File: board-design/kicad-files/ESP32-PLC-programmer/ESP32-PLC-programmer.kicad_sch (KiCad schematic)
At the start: 28 parts, among them J1 302-S101, J2 0473460001, J3 302-S101, U1 TPS62060DSGR, U2 FT231XS

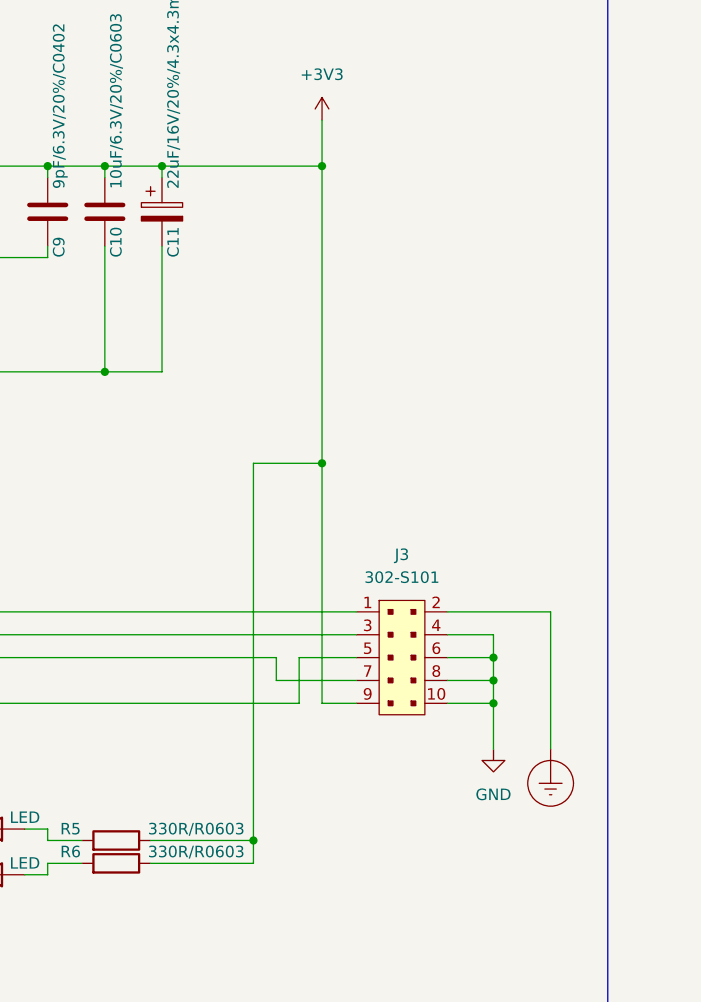
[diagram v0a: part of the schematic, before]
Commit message: [UPDATE]
Finished ESP32 and ESP32-programmer board designs (few corrections to be made when manufacturer is chosen - design rules).

Signed-off-by: Nicolae-Andrei Vasile <vasilenicolaeandrei@gmail.com>
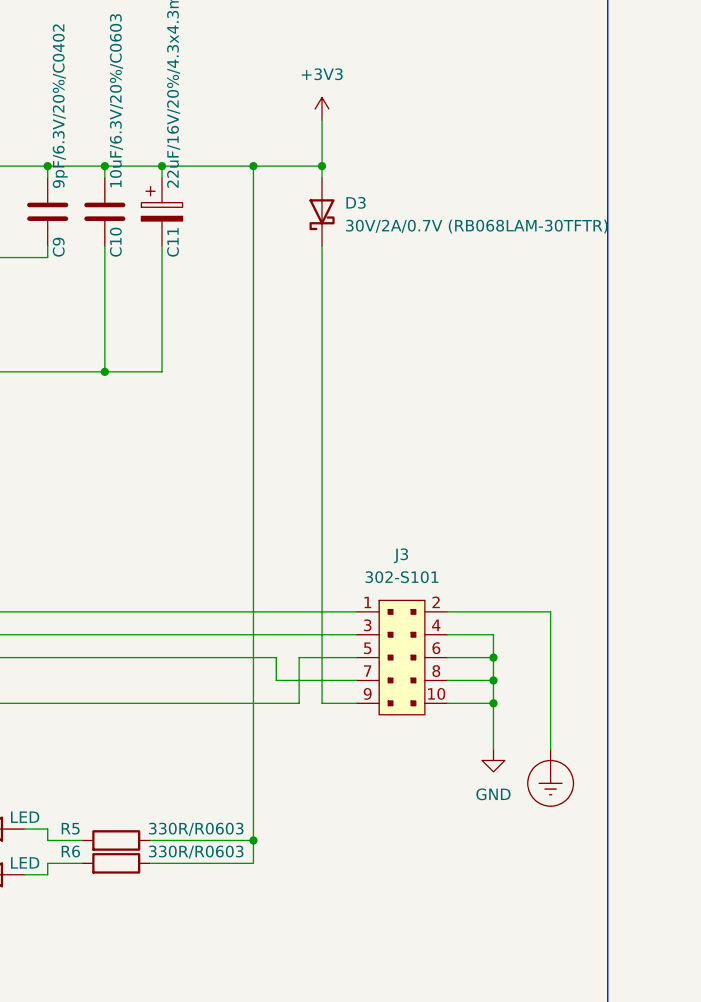
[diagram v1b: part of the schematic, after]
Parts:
- added D3: 30V/2A/0.7V (RB068LAM-30TFTR), Diode_SMD:D_SOD-128, symbol Device:D_Schottky
- J1, J3: footprint digikey-footprints:PinHeader_2x5_P2.54mm_Drill1.2mm -> Connector_IDC:IDC-Header_2x05_P2.54mm_Vertical
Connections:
- net +3V3: now also D3.2 (A); no longer J3.9
- new net: D3.1 (K), J3.9
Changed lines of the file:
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@@
   (junction (at 119.38 92.71) (diameter 0) (color 0 0 0 0)
   )
+  (junction (at 217.17 38.1) (diameter 0) (color 0 0 0 0)
+  )
+  (junction (at 113.03 132.08) (diameter 0) (color 0 0 0 0)
+  )
+  (junction (at 160.02 60.96) (diameter 0) (color 0 0 0 0)
+  )
+  (junction (at 195.58 38.1) (diameter 0) (color 0 0 0 0)
+  )
+  (junction (at 106.68 95.25) (diameter 0) (color 0 0 0 0)
+  )
+  (junction (at 80.01 132.08) (diameter 0) (color 0 0 0 0)
+  )
+  (junction (at 153.67 60.96) (diameter 0) (color 0 0 0 0)
+  )
+  (junction (at 254 92.71) (diameter 0) (color 0 0 0 0)
+  )
+  (junction (at 195.58 60.96) (diameter 0) (color 0 0 0 0)
+  )
+  (junction (at 227.33 113.03) (diameter 0) (color 0 0 0 0)
+  )
+  (junction (at 95.25 132.08) (diameter 0) (color 0 0 0 0)
+  )
+  (junction (at 119.38 132.08) (diameter 0) (color 0 0 0 0)
+  )
+  (junction (at 48.26 171.45) (diameter 0) (color 0 0 0 0)
+  )
+  (junction (at 125.73 77.47) (diameter 0) (color 0 0 0 0)
+  )
+  (junction (at 160.02 40.64) (diameter 0) (color 0 0 0 0)
+  )
+  (junction (at 210.82 60.96) (diameter 0) (color 0 0 0 0)
+  )
+  (junction (at 27.94 163.83) (diameter 0) (color 0 0 0 0)
+  )
+  (junction (at 27.94 173.99) (diameter 0) (color 0 0 0 0)
+  )
+  (junction (at 113.03 97.79) (diameter 0) (color 0 0 0 0)
+  )
+  (junction (at 160.02 38.1) (diameter 0) (color 0 0 0 0)
+  )
+  (junction (at 204.47 38.1) (diameter 0) (color 0 0 0 0)
+  )
+  (junction (at 227.33 38.1) (diameter 0) (color 0 0 0 0)
+  )
+  (junction (at 153.67 38.1) (diameter 0) (color 0 0 0 0)
+  )
   (junction (at 234.95 38.1) (diameter 0) (color 0 0 0 0)
-  )
-  (junction (at 217.17 38.1) (diameter 0) (color 0 0 0 0)
-  )
-  (junction (at 113.03 132.08) (diameter 0) (color 0 0 0 0)
-  )
-  (junction (at 160.02 60.96) (diameter 0) (color 0 0 0 0)
-  )
-  (junction (at 195.58 38.1) (diameter 0) (color 0 0 0 0)
-  )
-  (junction (at 106.68 95.25) (diameter 0) (color 0 0 0 0)
-  )
-  (junction (at 80.01 132.08) (diameter 0) (color 0 0 0 0)
-  )
-  (junction (at 153.67 60.96) (diameter 0) (color 0 0 0 0)
-  )
-  (junction (at 254 92.71) (diameter 0) (color 0 0 0 0)
-  )
-  (junction (at 195.58 60.96) (diameter 0) (color 0 0 0 0)
-  )
-  (junction (at 227.33 113.03) (diameter 0) (color 0 0 0 0)
-  )
-  (junction (at 95.25 132.08) (diameter 0) (color 0 0 0 0)
-  )
-  (junction (at 119.38 132.08) (diameter 0) (color 0 0 0 0)
-  )
-  (junction (at 48.26 171.45) (diameter 0) (color 0 0 0 0)
-  )
-  (junction (at 125.73 77.47) (diameter 0) (color 0 0 0 0)
-  )
-  (junction (at 160.02 40.64) (diameter 0) (color 0 0 0 0)
-  )
-  (junction (at 210.82 60.96) (diameter 0) (color 0 0 0 0)
-  )
-  (junction (at 27.94 163.83) (diameter 0) (color 0 0 0 0)
-  )
-  (junction (at 27.94 173.99) (diameter 0) (color 0 0 0 0)
-  )
-  (junction (at 113.03 97.79) (diameter 0) (color 0 0 0 0)
-  )
-  (junction (at 160.02 38.1) (diameter 0) (color 0 0 0 0)
-  )
-  (junction (at 204.47 38.1) (diameter 0) (color 0 0 0 0)
-  )
-  (junction (at 153.67 38.1) (diameter 0) (color 0 0 0 0)
-  )
-  (junction (at 234.95 71.12) (diameter 0) (color 0 0 0 0)
   )
   (junction (at 48.26 173.99) (diameter 0) (color 0 0 0 0)
@@
     (stroke (width 0) (type default))
   )
-  (wire (pts (xy 217.17 38.1) (xy 234.95 38.1))
+  (wire (pts (xy 217.17 38.1) (xy 227.33 38.1))
     (stroke (width 0) (type default))
   )
@@
     (stroke (width 0) (type default))
   )
+  (wire (pts (xy 227.33 38.1) (xy 234.95 38.1))
+    (stroke (width 0) (type default))
+  )
   (wire (pts (xy 170.18 80.01) (xy 170.18 77.47))
     (stroke (width 0) (type default))
@@
     (stroke (width 0) (type default))
   )
-  (wire (pts (xy 227.33 71.12) (xy 227.33 113.03))
+  (wire (pts (xy 227.33 38.1) (xy 227.33 113.03))
+    (stroke (width 0) (type default))
+  )
+  (wire (pts (xy 234.95 38.1) (xy 234.95 39.37))
     (stroke (width 0) (type default))
   )
@@
     (stroke (width 0) (type default))
   )
-  (wire (pts (xy 234.95 38.1) (xy 234.95 71.12))
-    (stroke (width 0) (type default))
-  )
   (wire (pts (xy 105.41 176.53) (xy 105.41 179.07))
     (stroke (width 0) (type default))
@@
     (stroke (width 0) (type default))
   )
-  (wire (pts (xy 227.33 71.12) (xy 234.95 71.12))
-    (stroke (width 0) (type default))
-  )
   (wire (pts (xy 193.04 113.03) (xy 190.5 113.03))
     (stroke (width 0) (type default))
@@
     (stroke (width 0) (type default))
   )
-  (wire (pts (xy 234.95 71.12) (xy 234.95 97.79))
+  (wire (pts (xy 234.95 46.99) (xy 234.95 97.79))
     (stroke (width 0) (type default))
   )
@@
       (effects (font (size 1.27 1.27)))
     )
-    (property "Footprint" "digikey-footprints:PinHeader_2x5_P2.54mm_Drill1.2mm" (at 248.92 87.63 0)
+    (property "Footprint" "Connector_IDC:IDC-Header_2x05_P2.54mm_Vertical" (at 248.92 87.63 0)
       (effects (font (size 1.524 1.524)) (justify left) hide)
     )
@@
     )
   )
+  (symbol (lib_id "Device:D_Schottky") (at 234.95 43.18 90) (unit 1)
+    (in_bom yes) (on_board yes) (dnp no) (fields_autoplaced)
+    (property "Reference" "D3" (at 237.49 42.2275 90)
+      (effects (font (size 1.27 1.27)) (justify right))
+    )
+    (property "Value" "30V/2A/0.7V (RB068LAM-30TFTR)" (at 237.49 44.7675 90)
+      (effects (font (size 1.27 1.27)) (justify right))
+    )
+    (property "Footprint" "Diode_SMD:D_SOD-128" (at 234.95 43.18 0)
+      (effects (font (size 1.27 1.27)) hide)
+    )
+    (property "Datasheet" "https://fscdn.rohm.com/en/products/databook/datasheet/discrete/diode/schottky_barrier/rb068lam-30tftr-e.pdf" (at 234.95 43.18 0)
+      (effects (font (size 1.27 1.27)) hide)
+    )
+    (pin "1")
+    (pin "2")
+    (instances
+      (project "ESP32-PLC-programmer"
+        (path "/61b509ff-cde0-4481-9daa-5e3d0d14c769"
+          (reference "D3") (unit 1)
+        )
+      )
+    )
+  )
   (symbol (lib_id "Device:LED") (at 198.12 116.84 0) (unit 1)
     (in_bom yes) (on_board yes) (dnp no)
@@
       (effects (font (size 1.27 1.27)))
     )
-    (property "Footprint" "digikey-footprints:PinHeader_2x5_P2.54mm_Drill1.2mm" (at 43.18 163.83 0)
-      (effects (font (size 1.524 1.524)) (justify left) hide)
-    )
+    (property "Footprint" "Connector_IDC:IDC-Header_2x05_P2.54mm_Vertical" (at 43.18 163.83 0)
+      (effects (font (size 1.524 1.524)) (justify left) hide)
+    )
